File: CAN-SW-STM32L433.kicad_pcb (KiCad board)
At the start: 2 copper layers, 70 x 47 mm, 29 parts, among them CON12V1 CENTER+, J1 CANBUS, J2 TERM, U1 STM32L433RCT3, U2 MCP2562-E-SN

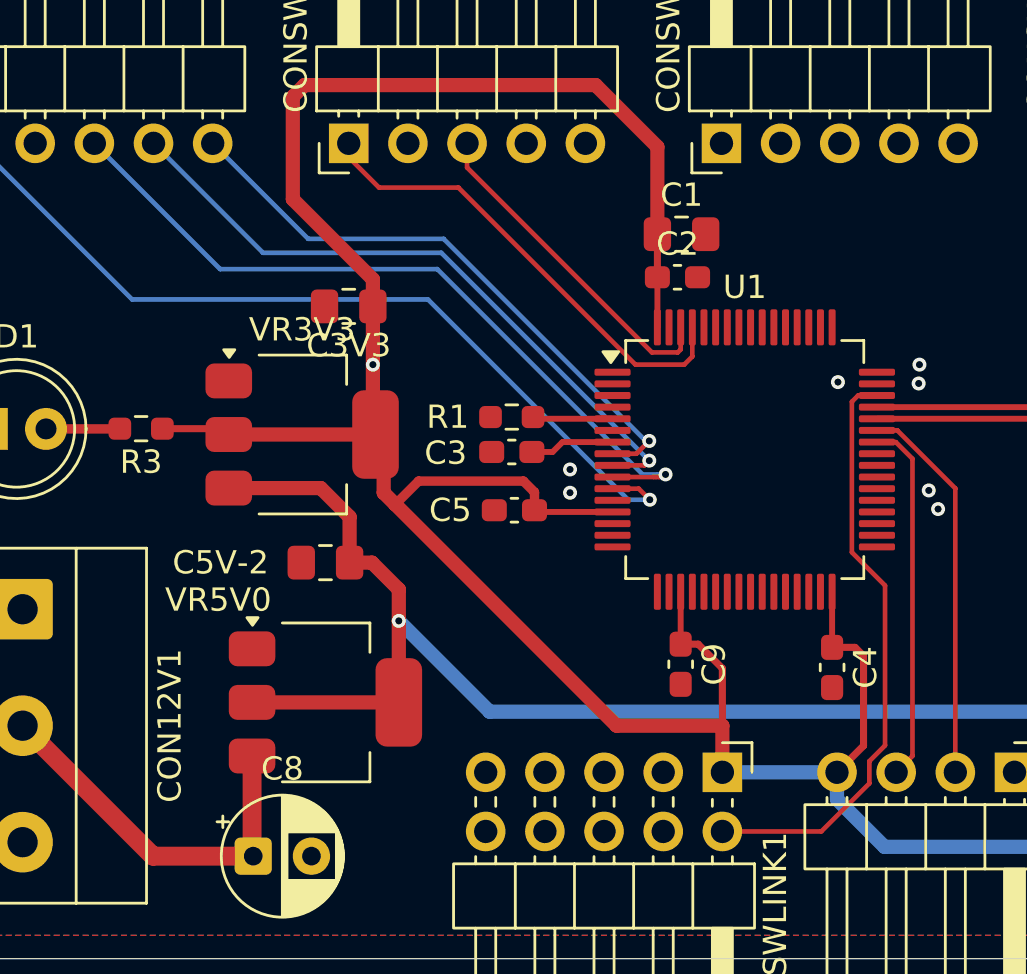
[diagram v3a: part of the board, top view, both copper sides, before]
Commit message: routing getting tricky with just two layers
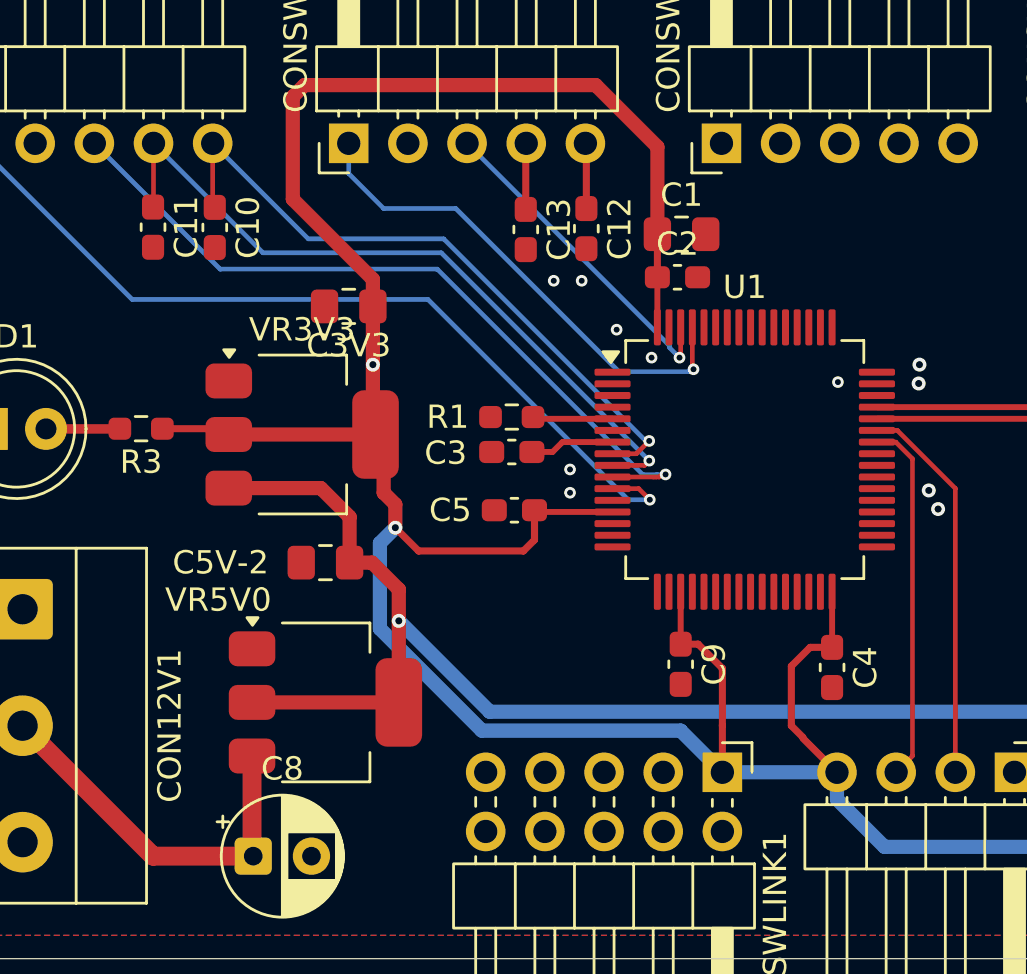
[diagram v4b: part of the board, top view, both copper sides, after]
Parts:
- added C10: 100n, Capacitor_SMD:C_0603_1608Metric_Pad1.08x0.95mm_HandSolder, F.Cu at (116.2, 91.6)
- added C11: 100n, Capacitor_SMD:C_0603_1608Metric_Pad1.08x0.95mm_HandSolder, F.Cu at (113.6, 91.6)
- added C12: 100n, Capacitor_SMD:C_0603_1608Metric_Pad1.08x0.95mm_HandSolder, F.Cu at (132.2, 91.7)
- added C13: 100n, Capacitor_SMD:C_0603_1608Metric_Pad1.08x0.95mm_HandSolder, F.Cu at (129.6, 91.7)
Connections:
- CONSW2 pad 4: /ADC1_IN4 -> /ADC1_IN6
- CONSW2 pad 5: /ADC1_IN3 -> /ADC1_IN5
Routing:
- net /SWDIO: track 25.6 -> 0.00 mm
- net +3.3V: track 147.1 -> 153.0 mm, vias 2 -> 3
- net /ADC1_IN6: track 0.00 -> 2.85 mm
- net /ADC1_IN5: track 0.00 -> 2.82 mm
- net /ADC1_IN1: track 25.8 -> 28.6 mm
- net /ADC1_IN2: track 29.1 -> 31.8 mm
- net /CTL2: track 20.4 -> 21.5 mm, vias 0 -> 1
- net /DEN2: track 14.5 -> 14.3 mm, vias 0 -> 1
- net GND: vias 14 -> 18

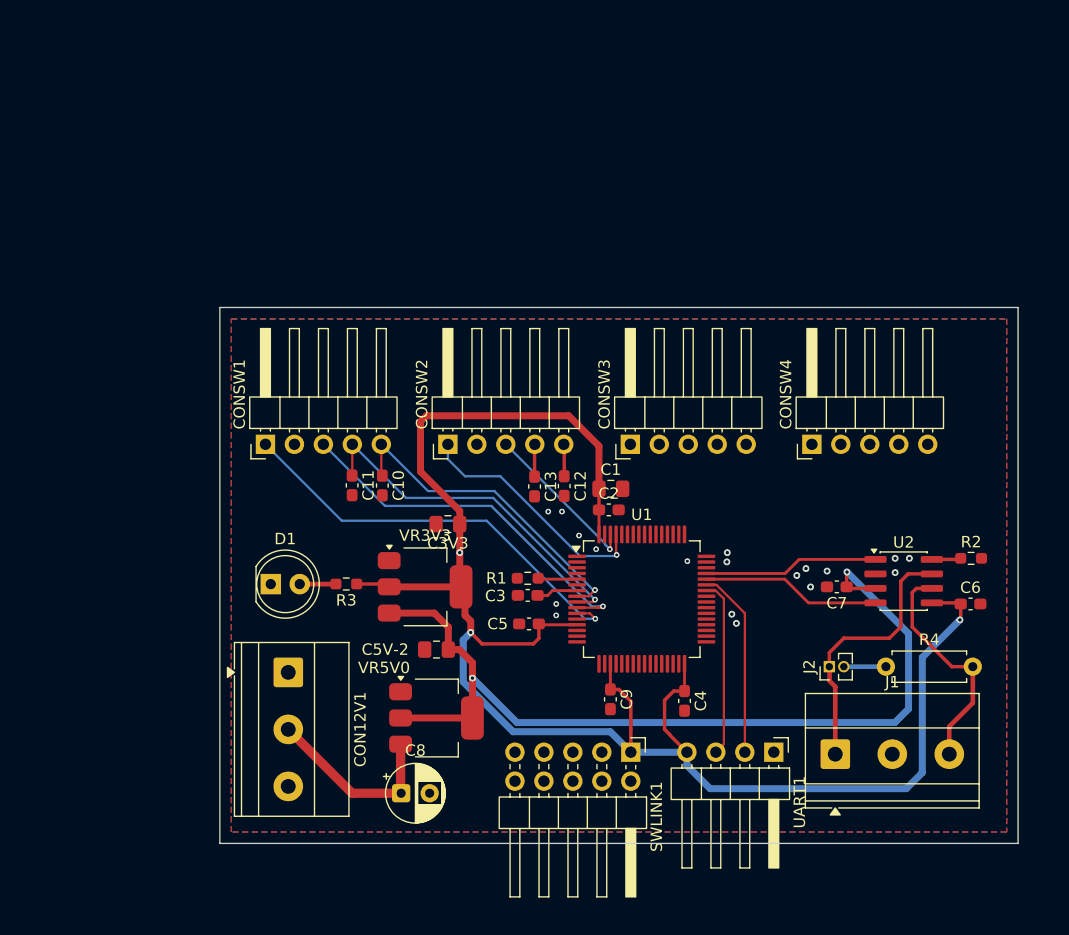
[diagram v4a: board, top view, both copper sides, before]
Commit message: layout mostly complete, working on DRC
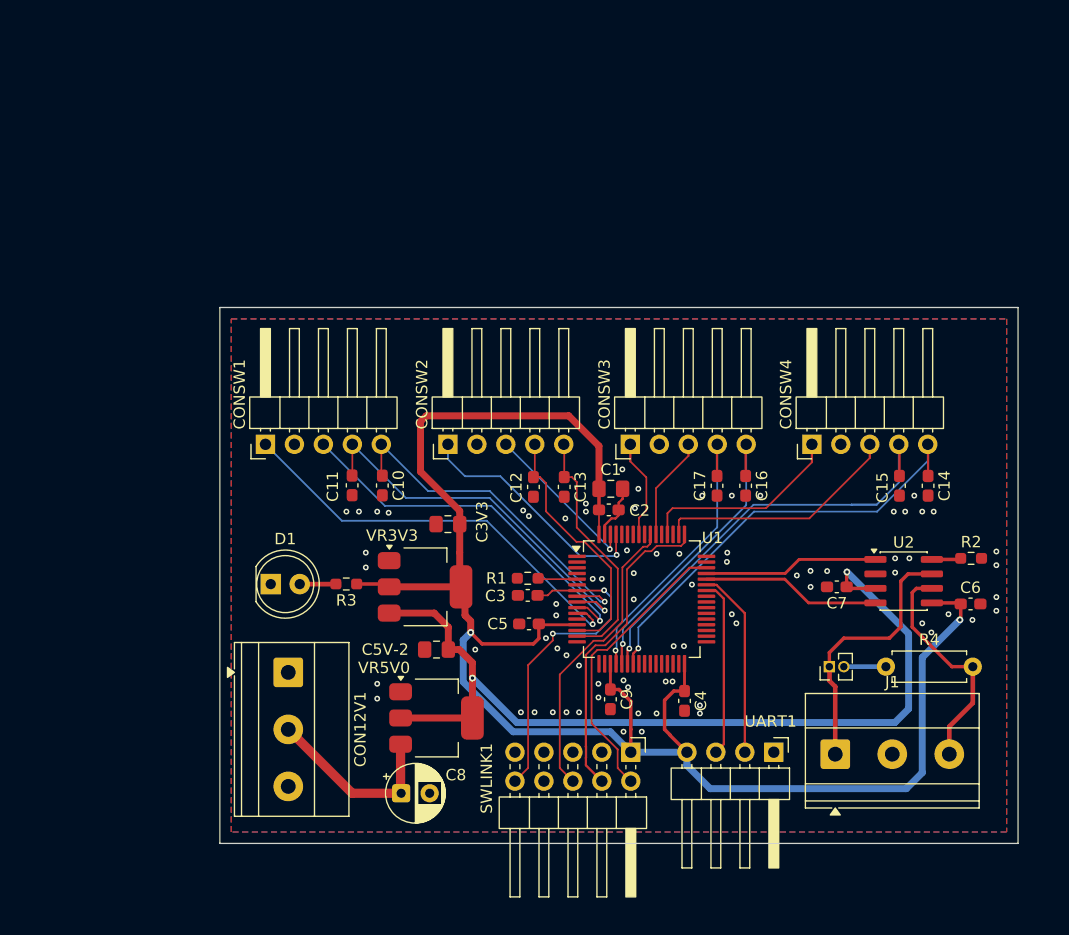
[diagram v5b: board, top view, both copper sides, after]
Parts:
- added C14: 100n, Capacitor_SMD:C_0603_1608Metric_Pad1.08x0.95mm_HandSolder, F.Cu at (164.1, 91.6)
- added C15: 100n, Capacitor_SMD:C_0603_1608Metric_Pad1.08x0.95mm_HandSolder, F.Cu at (161.6, 91.6)
- added C16: 100n, Capacitor_SMD:C_0603_1608Metric_Pad1.08x0.95mm_HandSolder, F.Cu at (148.1, 91.6)
- added C17: 100n, Capacitor_SMD:C_0603_1608Metric_Pad1.08x0.95mm_HandSolder, F.Cu at (145.6, 91.6)
- moved C12 2.70 mm to (129.5, 91.7)
- moved C13 2.60 mm to (132.2, 91.7)
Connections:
- CONSW2 pad 4: /ADC1_IN6 -> /ADC1_IN5
- CONSW2 pad 5: /ADC1_IN5 -> /ADC1_IN6
- CONSW3 pad 4: /IS3 -> /ADC1_IN9
- CONSW3 pad 5: /VS3 -> /ADC1_IN10
- CONSW4 pad 4: /IS4 -> /ADC1_IN11
- CONSW4 pad 5: /VS4 -> /ADC1_IN12
- U1 pad 50: unconnected-(U1-PA15-Pad50) -> /DEN4
- U1 pad 52: unconnected-(U1-PC11-Pad52) -> /CTL4
- U1 pad 54: unconnected-(U1-PD2-Pad54) -> /DEN3
- U1 pad 57: unconnected-(U1-PB5-Pad57) -> /CTL3
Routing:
- net /ADC1_IN12: track 0.00 -> 39.1 mm, vias 0 -> 1
- net /ADC1_IN11: track 0.00 -> 38.2 mm, vias 0 -> 1
- net /SWCLK: track 0.00 -> 27.9 mm
- net /SWO: track 0.00 -> 26.6 mm
- net /ADC1_IN10: track 0.00 -> 26.6 mm, vias 0 -> 1
- net /ADC1_IN9: track 0.00 -> 25.7 mm, vias 0 -> 1
- net /SWDIO: track 0.00 -> 25.7 mm
- net /NRST: track 3.64 -> 28.7 mm, vias 0 -> 2
- net /DEN4: track 0.00 -> 21.5 mm
- net /ADC1_IN5: track 2.82 -> 22.3 mm
- net /ADC1_IN6: track 2.85 -> 21.9 mm
- net /CTL4: track 0.00 -> 18.0 mm
- net /DEN3: track 0.00 -> 9.09 mm
- net /CTL3: track 0.00 -> 8.75 mm
- net GND: track 0.00 -> 4.86 mm, vias 18 -> 77
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
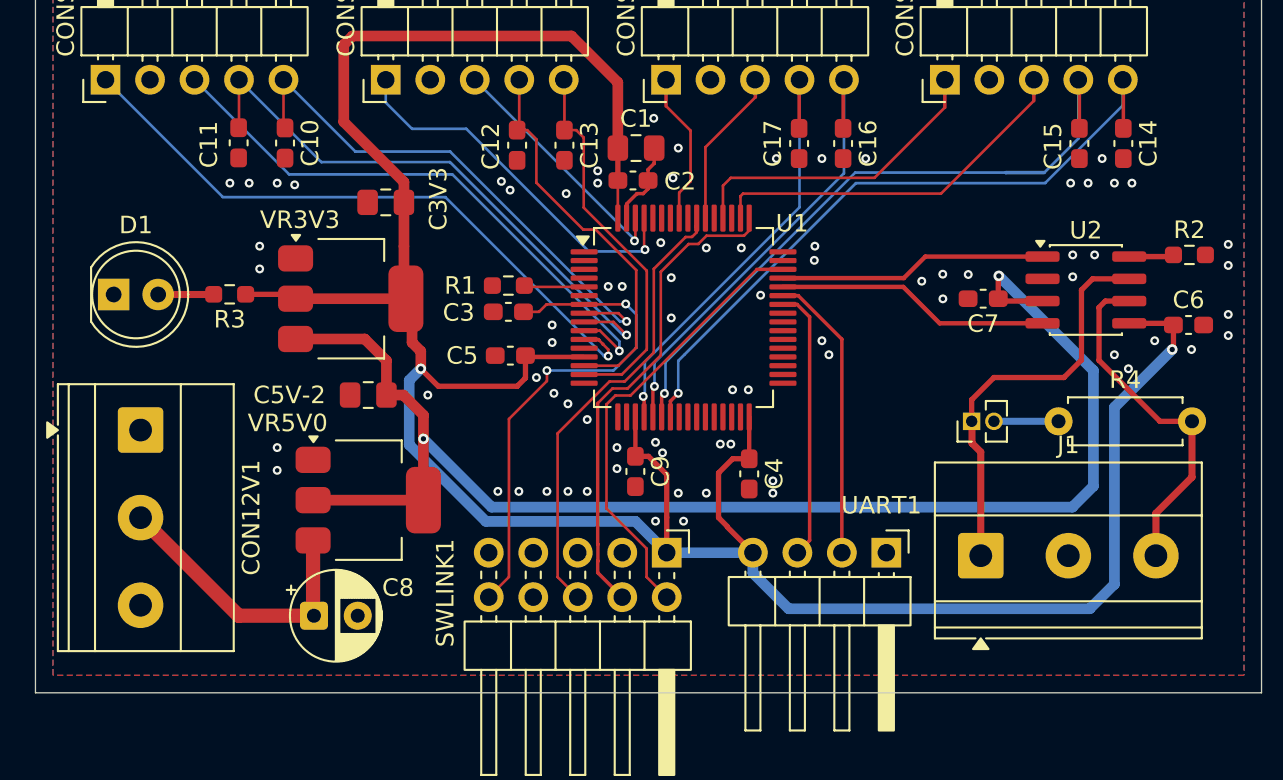
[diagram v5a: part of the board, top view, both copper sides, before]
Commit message: layout and drc complete, fix some silkscreen issues
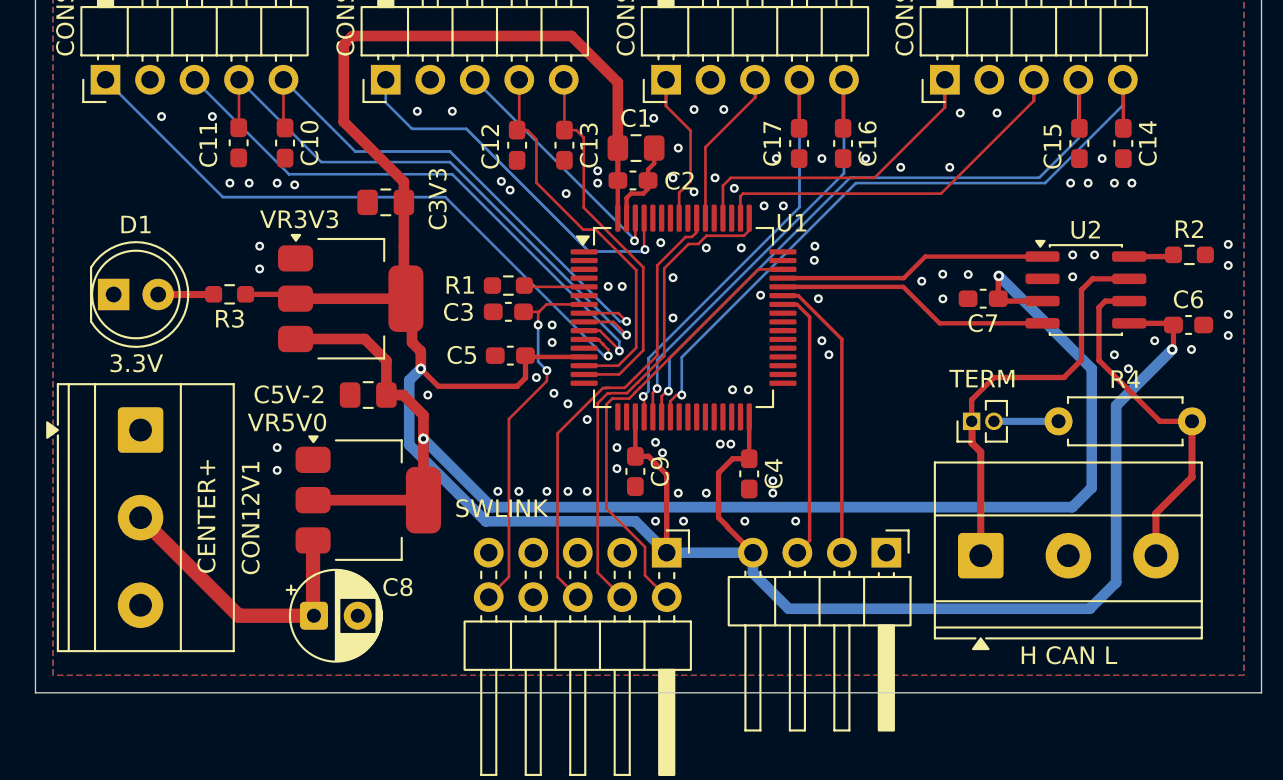
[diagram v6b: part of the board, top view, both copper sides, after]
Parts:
- J1: value CANBUS -> H CAN L
- J3: renamed from UART1; value Conn_01x04 -> UART1
- J4: renamed from SWLINK1; value Conn_ARM_JTAG_SWD_10 -> SWLINK
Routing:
- net /NRST: track 28.7 -> 21.5 mm
- net GND: track 4.86 -> 5.06 mm, vias 77 -> 95
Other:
- board text added: "(C) 2026 G MCLELLAN STM32 QUAD SWITCH CONTROL REV 01"

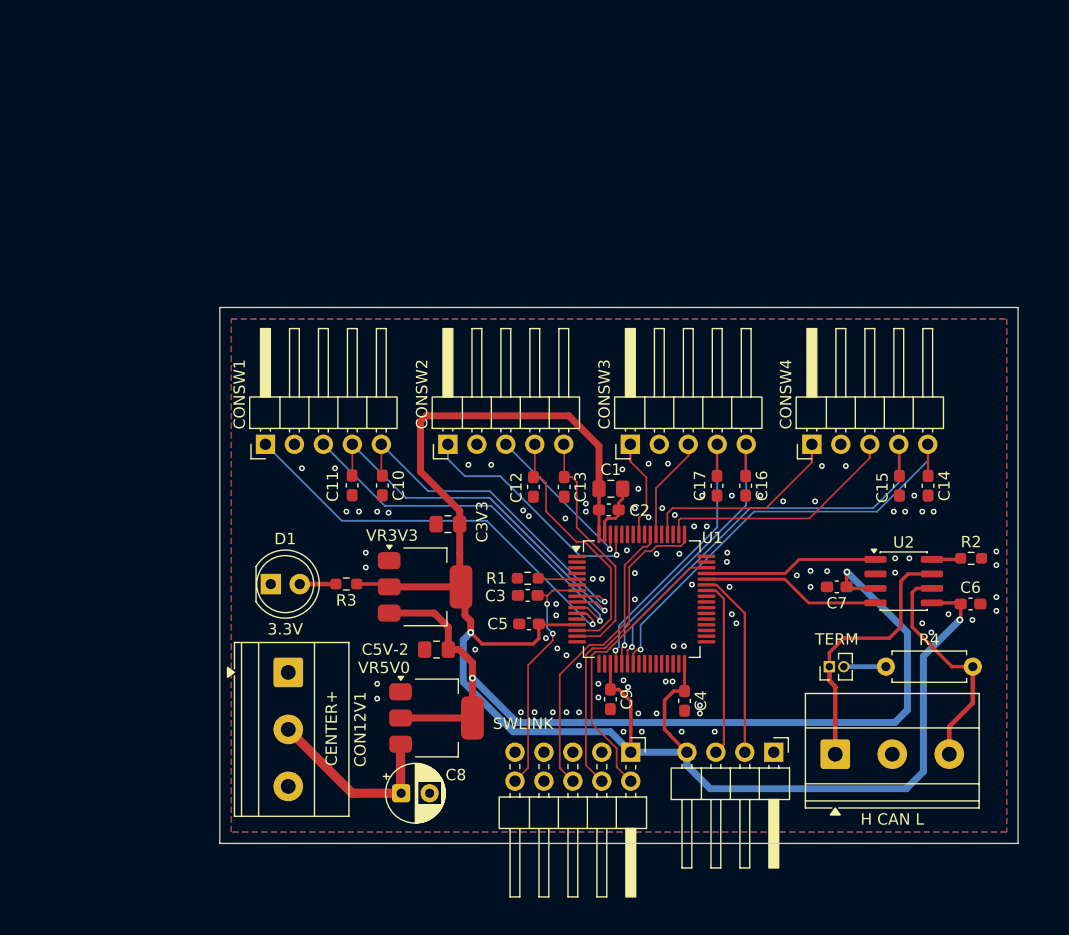
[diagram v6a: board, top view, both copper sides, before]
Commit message: moved power and can connectors, fixed some trace routing
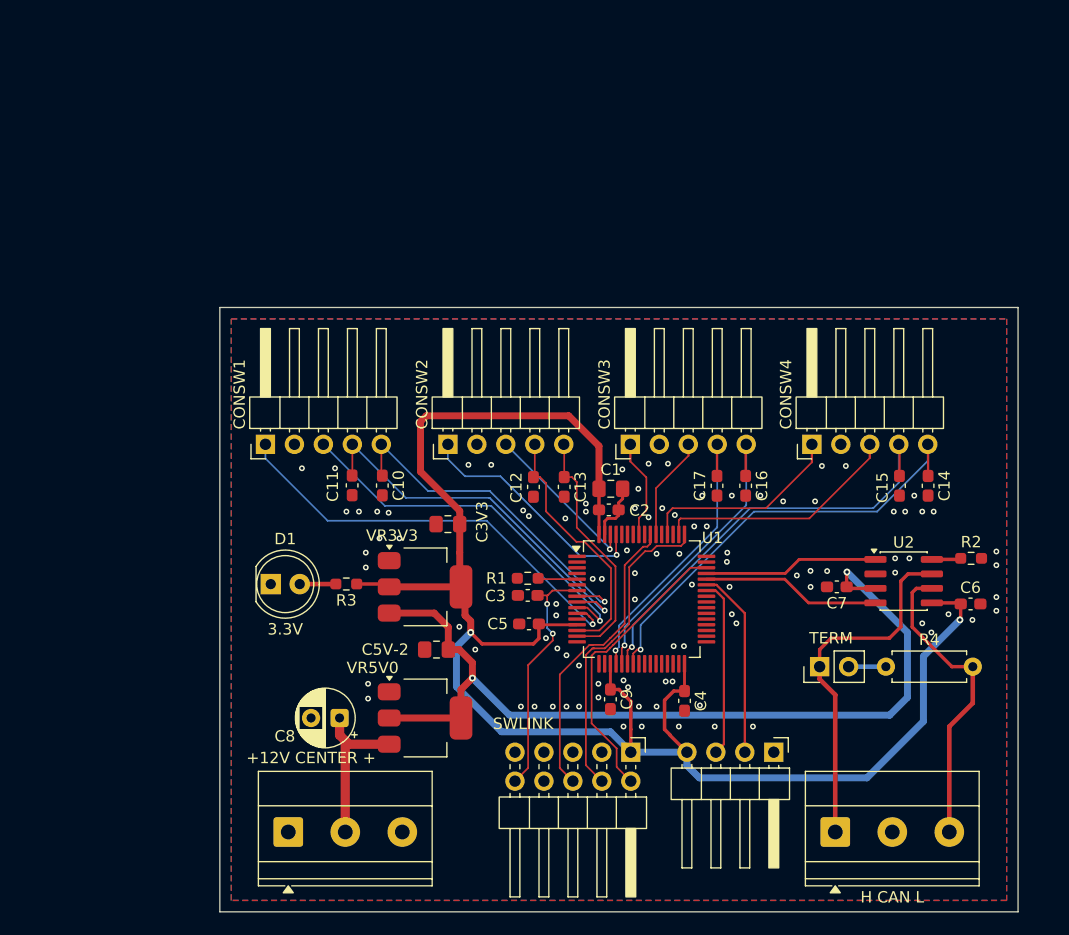
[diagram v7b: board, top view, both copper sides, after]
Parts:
- J2: footprint Connector_PinHeader_1.27mm:PinHeader_1x02_P1.27mm_Vertical -> Connector_PinHeader_2.54mm:PinHeader_1x02_P2.54mm_Vertical
- J5: renamed from CON12V1; value CENTER+ -> +12V CENTER +
- moved J5 14.0 mm to (108.0, 122.0), turned to 0 degrees
- moved C8 8.53 mm to (112.5, 112.0), turned to 180 degrees
- moved J1 6.83 mm to (156.0, 122.0)
- moved VR5V0 1.00 mm to (120.0, 112.0)
- moved J2 0.85 mm to (154.6, 107.5)
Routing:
- net /CANH: track 23.3 -> 31.5 mm
- net /CANL: track 20.2 -> 27.0 mm
- net +12V: track 16.5 -> 14.2 mm
- net +3.3V: track 153.0 -> 150.7 mm
- net +5V: track 79.8 -> 78.1 mm
- net /CTL1: track 37.2 -> 38.0 mm
- net GND: vias 95 -> 98
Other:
- board size 70 x 47 mm -> 70 x 53 mm

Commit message: silkscreen tweaks
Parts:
- J1: value H CAN L -> H GND L
- J5: value +12V CENTER + -> CENTER +12V
- renumbered C5V-2 to C5V0
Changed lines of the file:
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@@
 		(descr "Capacitor SMD 0805 (2012 Metric), square (rectangular) end terminal, IPC-7351 nominal with elongated pad for handsoldering. (Body size source: IPC-SM-782 page 76, https://www.pcb-3d.com/wordpress/wp-content/uploads/ipc-sm-782a_amendment_1_and_2.pdf, https://docs.google.com/spreadsheets/d/1BsfQQcO9C6DZCsRaXUlFlo91Tg2WpOkGARC1WS5S8t0/edit?usp=sharing), generated with kicad-footprint-generator")
 		(tags "capacitor handsolder")
-		(property "Reference" "C5V-2"
+		(property "Reference" "C5V0"
 			(at 4.5 0 0)
 			(layer "F.SilkS")
@@
 			)
 		)
-		(property "Value" "H CAN L"
+		(property "Value" "H GND L"
 			(at 5 5.72 0)
 			(layer "F.SilkS")
@@
 		(tags "capacitor handsolder")
 		(property "Reference" "C3V3"
-			(at -3 0.2 90)
+			(at -0.75 1.75 180)
 			(layer "F.SilkS")
 			(effects
@@
 			)
 		)
-		(property "Value" "+12V CENTER +"
-			(at 2 -6.5 180)
+		(property "Value" "CENTER +12V"
+			(at 5.5 6 180)
 			(layer "F.SilkS")
 			(effects
